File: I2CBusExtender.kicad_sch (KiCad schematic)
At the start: 7 parts

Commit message: Initial schematic.
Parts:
- removed R?: 10k, symbol Device:R
- added C? (x2): 1uF, symbol Device:C
- added D?: P6KE12A, symbol Device:D_TVS
- added R? (x2): 270R, symbol Device:R
- added R? (x3): 470, symbol Device:R
- added R? (x3): 10k, symbol Device:R
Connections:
- net at FB?.1: now also C?.1, D?.2 (A2)
- net at C?.1, C?.1, FB?.2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: now also R?.2, C?.1, R?.2, R?.2, R?.2, R?.2, R?.2, R?.2; no longer U?.6 (SCL)
- net at U?.7 (LCL): now also R?.1, R?.1; no longer R?.2
- net at R?.1, U?.2 (LDA): now also R?.1
- net at C?.2, C?.2, U?.4 (GND): now also C?.2, C?.2, D?.1 (A1)
- net at R?.1, U?.3 (SDA): now also R?.1, R?.1
- new net: R?.1, R?.1, R?.1, U?.6 (SCL)
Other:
- moved on the sheet: C?, FB?, R?, U?

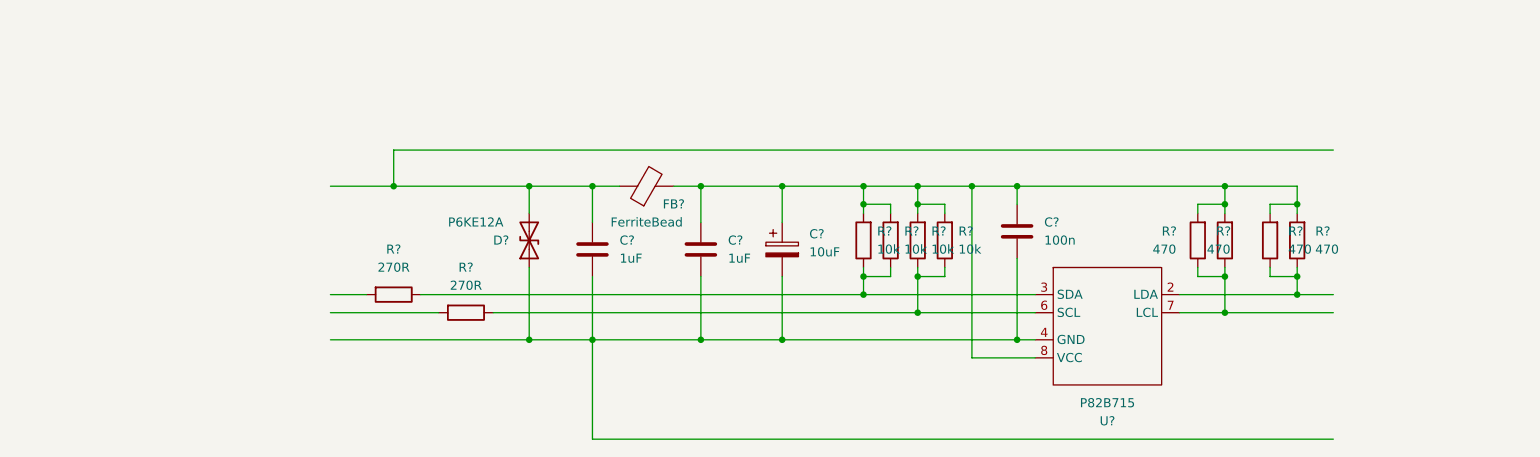
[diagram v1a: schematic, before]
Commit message: Initial layout and footprint adjustment complete.
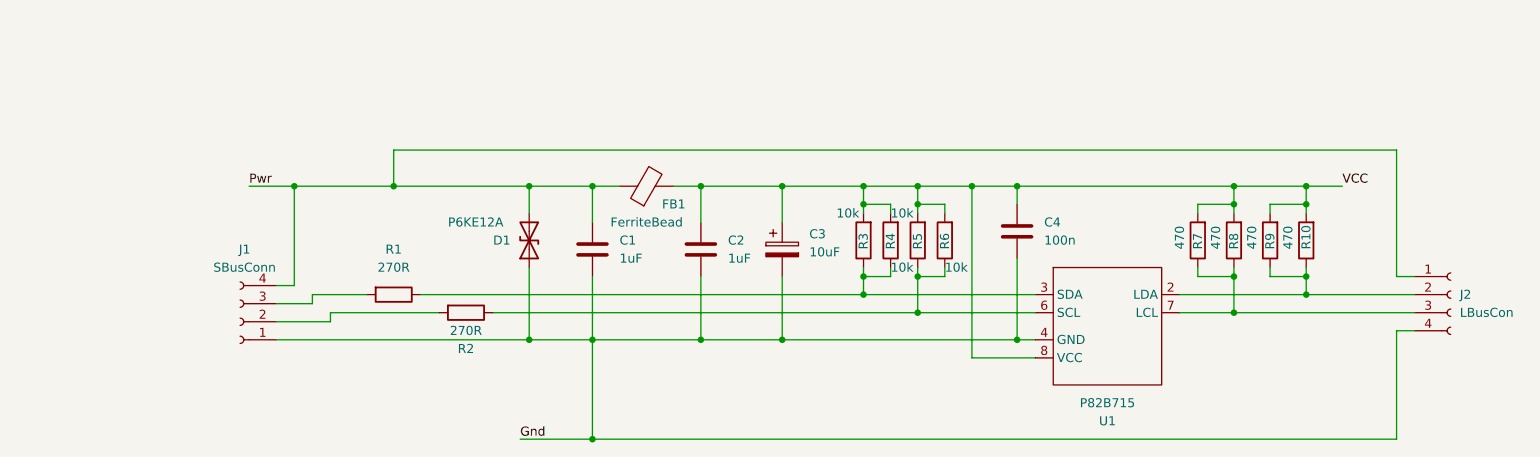
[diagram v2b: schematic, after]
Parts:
- removed R? (x2): 470, symbol Device:R
- added J1: SBusConn, Connector_Wire:SolderWire-0.5sqmm_1x04_P4.6mm_D0.9mm_OD2.1mm_Relief, symbol Connector:Conn_01x04_Female
- added J2: LBusCon, Connector_Wire:SolderWire-0.5sqmm_1x04_P4.6mm_D0.9mm_OD2.1mm_Relief, symbol Connector:Conn_01x04_Female
- added R10: 470, Resistor_THT:R_Axial_DIN0207_L6.3mm_D2.5mm_P5.08mm_Vertical, symbol Device:R
- added R9: 470, Resistor_SMD:R_1206_3216Metric_Pad1.30x1.75mm_HandSolder, symbol Device:R
- C1, C2, C4: renamed from C?; footprint (none) -> Capacitor_SMD:C_1206_3216Metric_Pad1.33x1.80mm_HandSolder
- C3: renamed from C?; footprint (none) -> Capacitor_THT:CP_Radial_D5.0mm_P2.00mm
- D1: renamed from D?; footprint (none) -> Diode_THT:D_DO-15_P12.70mm_Horizontal
- FB1: renamed from FB?; footprint (none) -> Diode_THT:D_DO-201AD_P3.81mm_Vertical_AnodeUp
- R1, R2: renamed from R?; footprint (none) -> Resistor_THT:R_Axial_DIN0207_L6.3mm_D2.5mm_P7.62mm_Horizontal
- R3, R5, R8: renamed from R?; footprint (none) -> Resistor_THT:R_Axial_DIN0207_L6.3mm_D2.5mm_P5.08mm_Vertical
- R4, R6, R7: renamed from R?; footprint (none) -> Resistor_SMD:R_1206_3216Metric_Pad1.30x1.75mm_HandSolder
- U1: renamed from U?; footprint (none) -> Package_SO:SO-8_3.9x4.9mm_P1.27mm
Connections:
- net at R1.2: now also J1.3 (Pin_3)
- net at R7.1, R8.1, U1.7 (LCL): now also J2.3 (Pin_3)
- net VCC: now reaches C2.1, C3.1, C4.1, FB1.2, R3.2, R4.2, R5.2, R6.2, R7.2, R8.2, U1.8 (VCC)
- net VCC: now also R10.2, R9.2
- net Pwr: now reaches C1.1, D1.2 (A2), FB1.1
- net Pwr: now also J1.4 (Pin_4), J2.1 (Pin_1)
- net at U1.2 (LDA): now also J2.2 (Pin_2), R10.1, R9.1
- net Gnd: now reaches C1.2, C2.2, C3.2, C4.2, D1.1 (A1), U1.4 (GND)
- net Gnd: now also J1.1 (Pin_1), J2.4 (Pin_4)
- net at R2.2: now also J1.2 (Pin_2)
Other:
- moved on the sheet: R8

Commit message: Tweaked schematic layout and improved board design to the point it passes DRC.
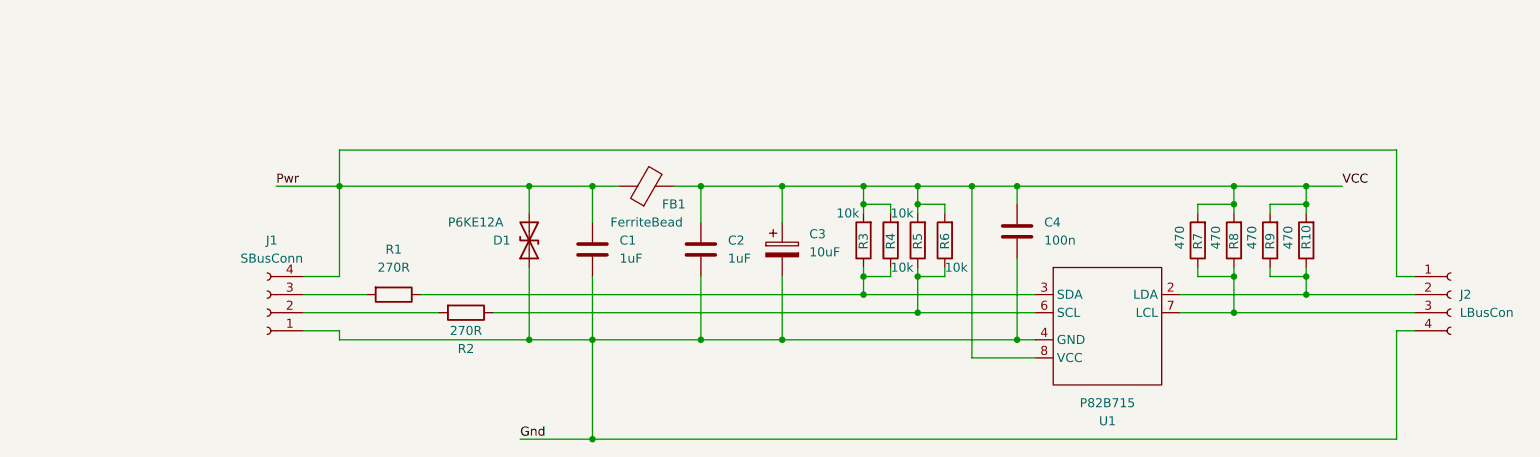
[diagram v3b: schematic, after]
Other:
- moved on the sheet: J1
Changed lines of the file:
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@@
   (junction (at 101.6 115.57) (diameter 0) (color 0 0 0 0)
   )
-  (junction (at 68.58 93.98) (diameter 0) (color 0 0 0 0)
-  )
   (junction (at 200.66 96.52) (diameter 0) (color 0 0 0 0)
   )
@@
   (junction (at 210.82 93.98) (diameter 0) (color 0 0 0 0)
   )
-  (junction (at 82.55 93.98) (diameter 0) (color 0 0 0 0)
-  )
   (junction (at 110.49 93.98) (diameter 0) (color 0 0 0 0)
   )
@@
   (junction (at 170.18 93.98) (diameter 0) (color 0 0 0 0)
   )
+  (junction (at 74.93 93.98) (diameter 0) (color 0 0 0 0)
+  )
   (junction (at 210.82 106.68) (diameter 0) (color 0 0 0 0)
   )
@@
     (stroke (width 0) (type default) (color 0 0 0 0))
   )
-  (wire (pts (xy 82.55 88.9) (xy 82.55 93.98))
+  (wire (pts (xy 74.93 88.9) (xy 74.93 93.98))
     (stroke (width 0) (type default) (color 0 0 0 0))
   )
@@
     (stroke (width 0) (type default) (color 0 0 0 0))
   )
-  (wire (pts (xy 82.55 88.9) (xy 223.52 88.9))
+  (wire (pts (xy 74.93 88.9) (xy 223.52 88.9))
     (stroke (width 0) (type default) (color 0 0 0 0))
   )
@@
     (stroke (width 0) (type default) (color 0 0 0 0))
   )
-  (wire (pts (xy 68.58 107.95) (xy 66.04 107.95))
+  (wire (pts (xy 74.93 106.68) (xy 69.85 106.68))
     (stroke (width 0) (type default) (color 0 0 0 0))
   )
@@
     (stroke (width 0) (type default) (color 0 0 0 0))
   )
-  (wire (pts (xy 82.55 93.98) (xy 101.6 93.98))
+  (wire (pts (xy 74.93 93.98) (xy 101.6 93.98))
     (stroke (width 0) (type default) (color 0 0 0 0))
   )
@@
     (stroke (width 0) (type default) (color 0 0 0 0))
   )
+  (wire (pts (xy 69.85 114.3) (xy 74.93 114.3))
+    (stroke (width 0) (type default) (color 0 0 0 0))
+  )
   (wire (pts (xy 210.82 109.22) (xy 226.06 109.22))
     (stroke (width 0) (type default) (color 0 0 0 0))
@@
     (stroke (width 0) (type default) (color 0 0 0 0))
   )
+  (wire (pts (xy 74.93 114.3) (xy 74.93 115.57))
+    (stroke (width 0) (type default) (color 0 0 0 0))
+  )
   (wire (pts (xy 156.21 106.68) (xy 156.21 111.76))
     (stroke (width 0) (type default) (color 0 0 0 0))
@@
     (stroke (width 0) (type default) (color 0 0 0 0))
   )
-  (wire (pts (xy 66.04 115.57) (xy 101.6 115.57))
+  (wire (pts (xy 74.93 115.57) (xy 101.6 115.57))
     (stroke (width 0) (type default) (color 0 0 0 0))
   )
@@
     (stroke (width 0) (type default) (color 0 0 0 0))
   )
-  (wire (pts (xy 73.66 113.03) (xy 66.04 113.03))
-    (stroke (width 0) (type default) (color 0 0 0 0))
-  )
   (wire (pts (xy 195.58 106.68) (xy 200.66 106.68))
     (stroke (width 0) (type default) (color 0 0 0 0))
@@
     (stroke (width 0) (type default) (color 0 0 0 0))
   )
-  (wire (pts (xy 68.58 93.98) (xy 68.58 107.95))
+  (wire (pts (xy 74.93 93.98) (xy 74.93 106.68))
     (stroke (width 0) (type default) (color 0 0 0 0))
   )
@@
     (stroke (width 0) (type default) (color 0 0 0 0))
   )
-  (wire (pts (xy 71.12 110.49) (xy 66.04 110.49))
-    (stroke (width 0) (type default) (color 0 0 0 0))
-  )
   (wire (pts (xy 110.49 106.68) (xy 110.49 115.57))
     (stroke (width 0) (type default) (color 0 0 0 0))
@@
     (stroke (width 0) (type default) (color 0 0 0 0))
   )
+  (wire (pts (xy 69.85 111.76) (xy 88.9 111.76))
+    (stroke (width 0) (type default) (color 0 0 0 0))
+  )
   (wire (pts (xy 101.6 115.57) (xy 110.49 115.57))
     (stroke (width 0) (type default) (color 0 0 0 0))
   )
-  (wire (pts (xy 71.12 109.22) (xy 78.74 109.22))
-    (stroke (width 0) (type default) (color 0 0 0 0))
-  )
-  (wire (pts (xy 68.58 93.98) (xy 82.55 93.98))
-    (stroke (width 0) (type default) (color 0 0 0 0))
-  )
   (wire (pts (xy 137.16 106.68) (xy 137.16 115.57))
     (stroke (width 0) (type default) (color 0 0 0 0))
@@
     (stroke (width 0) (type default) (color 0 0 0 0))
   )
-  (wire (pts (xy 62.23 93.98) (xy 68.58 93.98))
+  (wire (pts (xy 66.04 93.98) (xy 74.93 93.98))
     (stroke (width 0) (type default) (color 0 0 0 0))
   )
@@
     (stroke (width 0) (type default) (color 0 0 0 0))
   )
-  (wire (pts (xy 71.12 109.22) (xy 71.12 110.49))
+  (wire (pts (xy 69.85 109.22) (xy 78.74 109.22))
     (stroke (width 0) (type default) (color 0 0 0 0))
   )
@@
     (stroke (width 0) (type default) (color 0 0 0 0))
   )
-  (wire (pts (xy 73.66 111.76) (xy 88.9 111.76))
-    (stroke (width 0) (type default) (color 0 0 0 0))
-  )
   (wire (pts (xy 137.16 115.57) (xy 170.18 115.57))
     (stroke (width 0) (type default) (color 0 0 0 0))
@@
     (stroke (width 0) (type default) (color 0 0 0 0))
   )
-  (wire (pts (xy 73.66 111.76) (xy 73.66 113.03))
-    (stroke (width 0) (type default) (color 0 0 0 0))
-  )
   (wire (pts (xy 125.73 115.57) (xy 137.16 115.57))
     (stroke (width 0) (type default) (color 0 0 0 0))
@@
     (stroke (width 0) (type default) (color 0 0 0 0))
   )
-  (label "Pwr" (at 62.23 93.98 0)
+  (label "Pwr" (at 66.04 93.98 0)
     (effects (font (size 1.27 1.27)) (justify left bottom))
   )
@@
     (pin "2")
   )
-  (symbol (lib_id "Connector:Conn_01x04_Female") (at 60.96 113.03 180) (unit 1)
+  (symbol (lib_id "Connector:Conn_01x04_Female") (at 64.77 111.76 180) (unit 1)
     (in_bom yes) (on_board yes) (fields_autoplaced)
-    (property "Reference" "J1" (id 0) (at 61.595 102.87 0))
-    (property "Value" "SBusConn" (id 1) (at 61.595 105.41 0))
-    (property "Footprint" "Connector_Wire:SolderWire-0.5sqmm_1x04_P4.6mm_D0.9mm_OD2.1mm_Relief" (id 2) (at 60.96 113.03 0)
-      (effects (font (size 1.27 1.27)) hide)
-    )
-    (property "Datasheet" "~" (id 3) (at 60.96 113.03 0)
-      (effects (font (size 1.27 1.27)) hide)
-    )
+    (property "Reference" "J1" (id 0) (at 65.405 101.6 0))
+    (property "Value" "SBusConn" (id 1) (at 65.405 104.14 0))
+    (property "Footprint" "Connector_Wire:SolderWire-0.5sqmm_1x04_P4.6mm_D0.9mm_OD2.1mm_Relief" (id 2) (at 64.77 111.76 0)
+      (effects (font (size 1.27 1.27)) hide)
+    )
+    (property "Datasheet" "~" (id 3) (at 64.77 111.76 0)
+      (effects (font (size 1.27 1.27)) hide)
+    )

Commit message: Tweaked layouts and footprints.
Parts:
- FB1: footprint Diode_THT:D_DO-201AD_P3.81mm_Vertical_AnodeUp -> Diode_THT:D_DO-201AD_P5.08mm_Vertical_AnodeUp
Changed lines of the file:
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@@
     (property "Reference" "FB1" (id 0) (at 121.92 96.52 90))
     (property "Value" "FerriteBead" (id 1) (at 118.11 99.06 90))
-    (property "Footprint" "Diode_THT:D_DO-201AD_P3.81mm_Vertical_AnodeUp" (id 2) (at 118.11 95.758 90)
+    (property "Footprint" "Diode_THT:D_DO-201AD_P5.08mm_Vertical_AnodeUp" (id 2) (at 118.11 95.758 90)
       (effects (font (size 1.27 1.27)) hide)
     )
@@
     )
     (path "/16dced80-e89f-4732-a9d0-2ec4769624b0"
-      (reference "FB1") (unit 1) (value "FerriteBead") (footprint "Diode_THT:D_DO-201AD_P3.81mm_Vertical_AnodeUp")
+      (reference "FB1") (unit 1) (value "FerriteBead") (footprint "Diode_THT:D_DO-201AD_P5.08mm_Vertical_AnodeUp")
     )
     (path "/229a9edf-f2f6-4480-8389-16c61feed870"
